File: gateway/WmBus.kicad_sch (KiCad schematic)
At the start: 9 parts, among them IC1201 MIC5317-3.3xM5

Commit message: Working on version 1.0
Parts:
- added C1203, C1204: 100n, Capacitor_SMD:C_0805_2012Metric, symbol Device:C
- added IC1202: TXU0102, Package_SO:VSSOP-8_2.3x2mm_P0.5mm, symbol Texas Instruments:TXU0102
- added M1201: iM891A-XL, IMST:iM891A-XL, symbol IMST:iM891A-XL
- added Q1201: BSS123, Package_TO_SOT_SMD:SOT-23, symbol Transistor_FET:BSS123
- added R1203, R1204, R1206, R1207: 0R, Resistor_SMD:R_0805_2012Metric, symbol Device:R
- added R1205, R1208: 10k, Resistor_SMD:R_0805_2012Metric, symbol Device:R
- added TP1203, TP1204, TP1205, TP1206: ~, Testpoints_Kampi:TestPoint_Pad_1.0x1.0mm, symbol Connector:TestPoint
- C1201, C1202: footprint (none) -> Capacitor_SMD:C_0805_2012Metric; manf (none) -> KYOCERA AVX; manf# (none) -> 08056C105MAT2A; mouser# (none) -> 581-08056C105MAT2A
- IC1201: manf (none) -> Microchip Technology; manf# (none) -> MIC5317-3.3YM5-TR; mouser# (none) -> 998-MIC5317-3.3YM5-TR
- R1201: footprint (none) -> Resistor_SMD:R_0805_2012Metric; manf (none) -> Bourns; manf# (none) -> CR0805-FX-1002GLF; mouser# (none) -> 652-CR0805-FX-1002GLF
- R1202: manf# CR0402-JW-680GLF -> CR0805-JW-680GLF; mouser# 652-CR0402-JW-680GLF -> 652-CR0805-JW-680GLF
- TP1201, TP1202: footprint (none) -> Testpoints_Kampi:TestPoint_Pad_1.0x1.0mm
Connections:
- net +3V3: now also C1204.1, IC1202.7 (VCCB), M1201.29 (VDD), R1208.1
- net GND: now also C1203.2, C1204.2, IC1202.2 (GND), M1201.15 (GND), M1201.17 (GND), M1201.24 (GND), M1201.28 (GND), M1201.30 (GND), M1201.31 (GND), M1201.32 (GND), M1201.33 (GND), M1201.34 (GND), M1201.35 (GND), M1201.5 (GND), Q1201.2 (S), R1205.2
- net wm-Bus-Power-Enable renamed wM-Bus-Power-Enable
- new net: M1201.25 (~{RESET}), Q1201.3 (D), R1208.2, TP1204.1
- new net: M1201.18 (RxD), R1207.2, TP1206.1
- new net: IC1202.8 (B1), R1206.1
- new net: M1201.19 (TxD), R1206.2, TP1205.1
- new net: IC1202.1 (B2), R1207.1
- new net: IC1202.4 (A2), R1204.2
- new net: IC1202.5 (A1), R1203.2
- new net +1V8: C1203.1, IC1202.3 (VCCA), IC1202.6 (OE)
- new net wM-Bus.Reset: Q1201.1 (G), R1205.1, TP1203.1
- new net wM-Bus.RxD: R1204.1
- new net wM-Bus.TxD: R1203.1
- no-connect marks 1 -> 5
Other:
- moved on the sheet: LED1201, R1202

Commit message: Working on PCB
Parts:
- added MP1201: (no value), Bivar:SLP3-300-100-F, symbol Mechanical_Kampi:Light_Pipe

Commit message: Working on version 1.0.0
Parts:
- removed IC1202: TXU0102, Package_SO:VSSOP-8_2.3x2mm_P0.5mm, symbol Texas Instruments:TXU0102
- added IC1202: TXB0104RUT, Package_DFN_QFN:Texas_R-PUQFN-N12, symbol Logic_LevelTranslator:TXB0104RUT
- R1203, R1204: now not fitted; now left out of the parts list
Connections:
- net +1V8: now also C1204.1, IC1202.1 (VCCA), IC1202.12 (OE); no longer C1203.1
- net +3V3: now also C1203.1, IC1202.11 (VCCB); no longer C1204.1
- net GND: now also IC1202.6 (GND)
- net wM-Bus.RxD: now also R1207.1; no longer R1204.1
- net wM-Bus.TxD: now also R1206.1; no longer R1203.1
- net at M1201.18 (RxD), TP1206.1: now also IC1202.9 (B2); no longer R1207.2
- net at M1201.19 (TxD), TP1205.1: now also IC1202.10 (B1); no longer R1206.2
- net at R1204.2: now also IC1202.5 (A4)
- net at R1203.2: now also IC1202.4 (A3)
- new net: IC1202.3 (A2), R1207.2
- new net: IC1202.2 (A1), R1206.2
- new net wM-Bus.CTS: R1204.1
- new net wM-Bus.RTS: R1203.1
- no-connect marks 5 -> 7

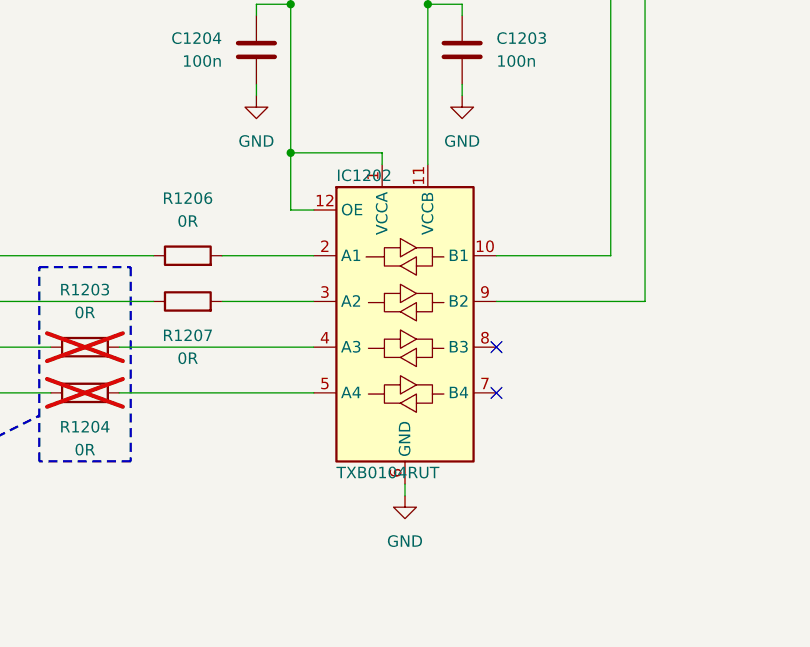
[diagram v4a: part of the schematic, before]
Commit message: Adding level shifter, update documentation
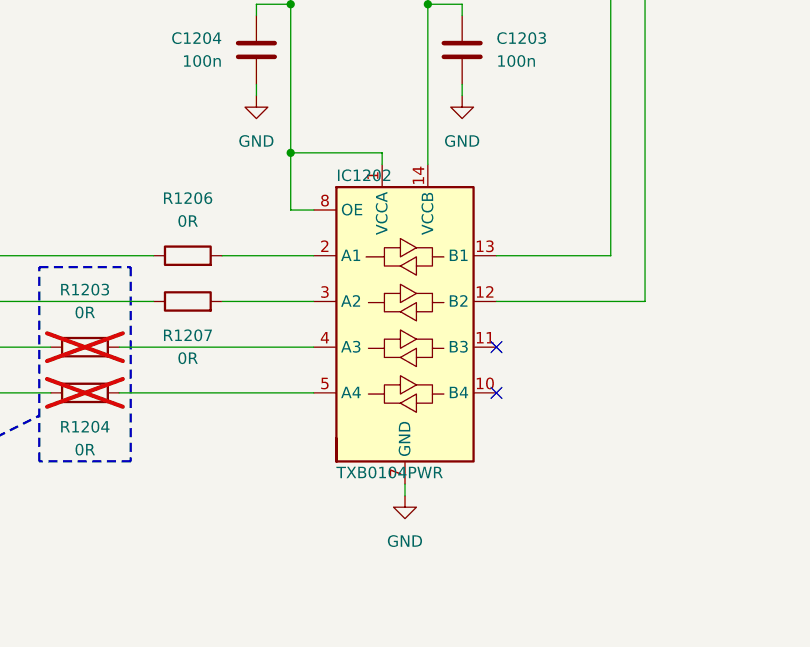
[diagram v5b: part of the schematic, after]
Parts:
- IC1202: value TXB0104RUT -> TXB0104PWR; footprint Package_DFN_QFN:Texas_R-PUQFN-N12 -> Package_SO:TSSOP-14_4.4x5mm_P0.65mm; symbol Logic_LevelTranslator:TXB0104RUT -> Logic_LevelTranslator:TXB0104PW; manf# TXB0104RUTR -> TXB0104PWR; mouser# 595-TXB0104RUTR -> 595-TXB0104PWR
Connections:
- net +1V8: now also IC1202.8 (OE); no longer IC1202.12 (OE)
- net +3V3: now also IC1202.14 (VCCB); no longer IC1202.11 (VCCB)
- net GND: now also IC1202.7 (GND); no longer IC1202.6 (GND)
- net at M1201.18 (RxD), TP1206.1: now also IC1202.12 (B2); no longer IC1202.9 (B2)
- net at M1201.19 (TxD), TP1205.1: now also IC1202.13 (B1); no longer IC1202.10 (B1)
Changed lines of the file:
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@@
 	)
 	(symbol
-		(lib_id "Logic_LevelTranslator:TXB0104RUT")
+		(lib_id "Logic_LevelTranslator:TXB0104PW")
 		(at 185.42 176.53 0)
 		(unit 1)
@@
 			)
 		)
-		(property "Value" "TXB0104RUT"
+		(property "Value" "TXB0104PWR"
 			(at 177.8 193.04 0)
 			(show_name no)
@@
 			)
 		)
-		(property "Footprint" "Package_DFN_QFN:Texas_R-PUQFN-N12"
+		(property "Footprint" "Package_SO:TSSOP-14_4.4x5mm_P0.65mm"
 			(at 185.42 195.58 0)
 			(hide yes)
@@
 			)
 		)
-		(property "Description" "4-Bit Bidirectional Voltage-Level Translator, Auto Direction Sensing and ±15-kV ESD Protection, 1.2 - 3.6V APort, 1.65 - 5.5V BPort, Texas_PUQFN-12"
+		(property "Description" "4-Bit Bidirectional Voltage-Level Translator, Auto Direction Sensing and ±15-kV ESD Protection, 1.2 - 3.6V APort, 1.65 - 5.5V BPort, TSSOP-14"
 			(at 185.42 176.53 0)
 			(hide yes)
@@
 			)
 		)
-		(property "manf#" "TXB0104RUTR"
+		(property "manf#" "TXB0104PWR"
 			(at 185.42 176.53 0)
 			(hide yes)
@@
 			)
 		)
-		(property "mouser#" "595-TXB0104RUTR"
+		(property "mouser#" "595-TXB0104PWR"
 			(at 185.42 176.53 0)
 			(hide yes)
@@
 		(pin "8"
 		)
+		(pin "13"
+		)
+		(pin "14"
+		)
 		(instances

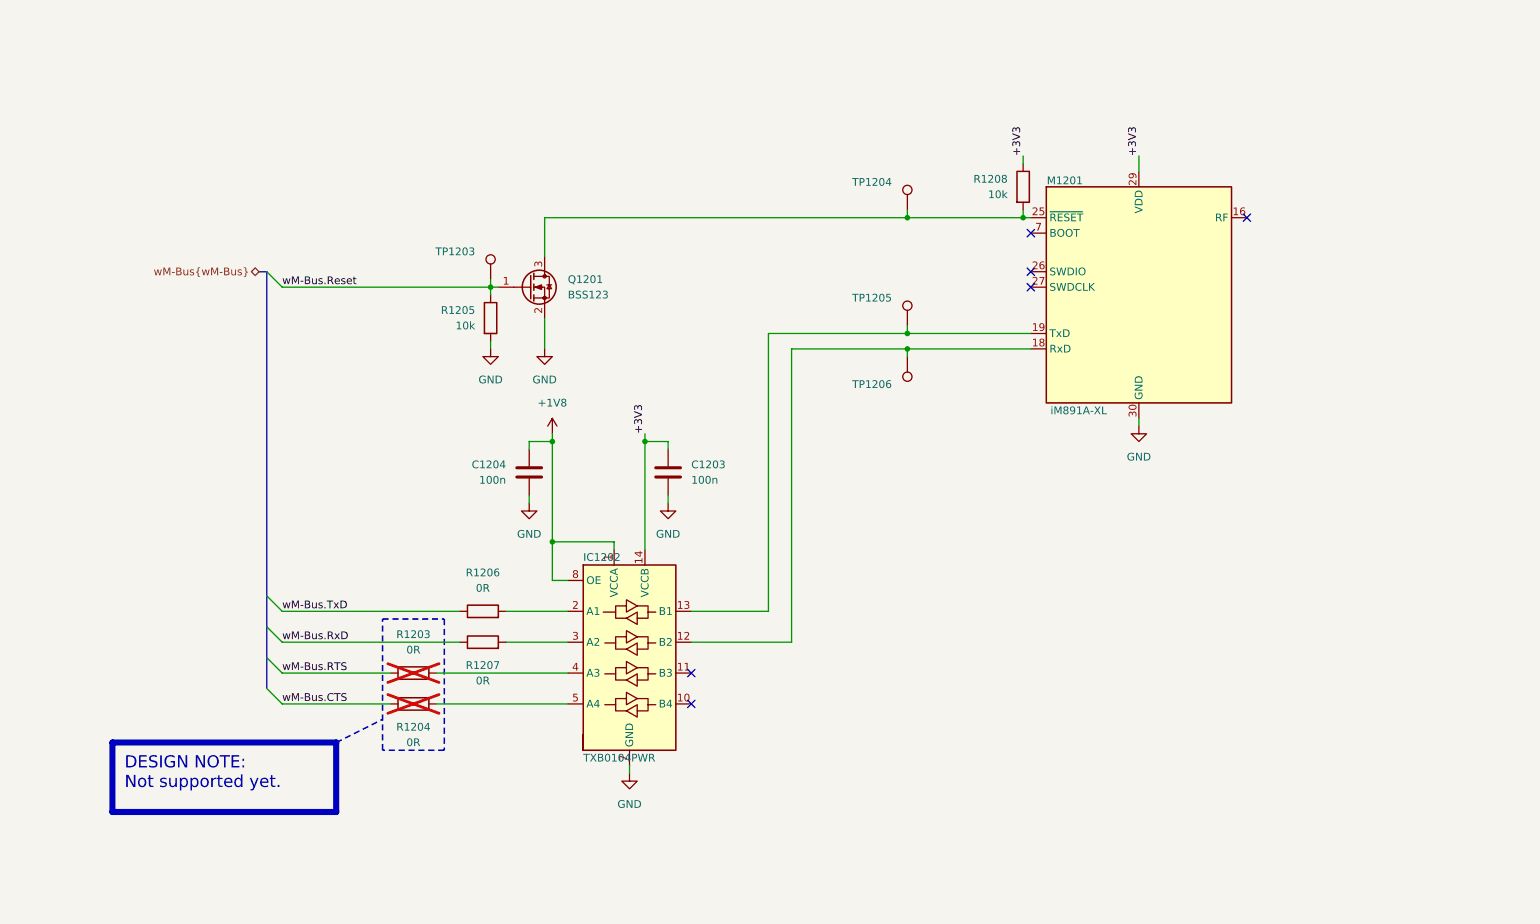
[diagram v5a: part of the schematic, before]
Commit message: Replace level shifter, replace CC2530 with CC2652, fix wrong part numbers
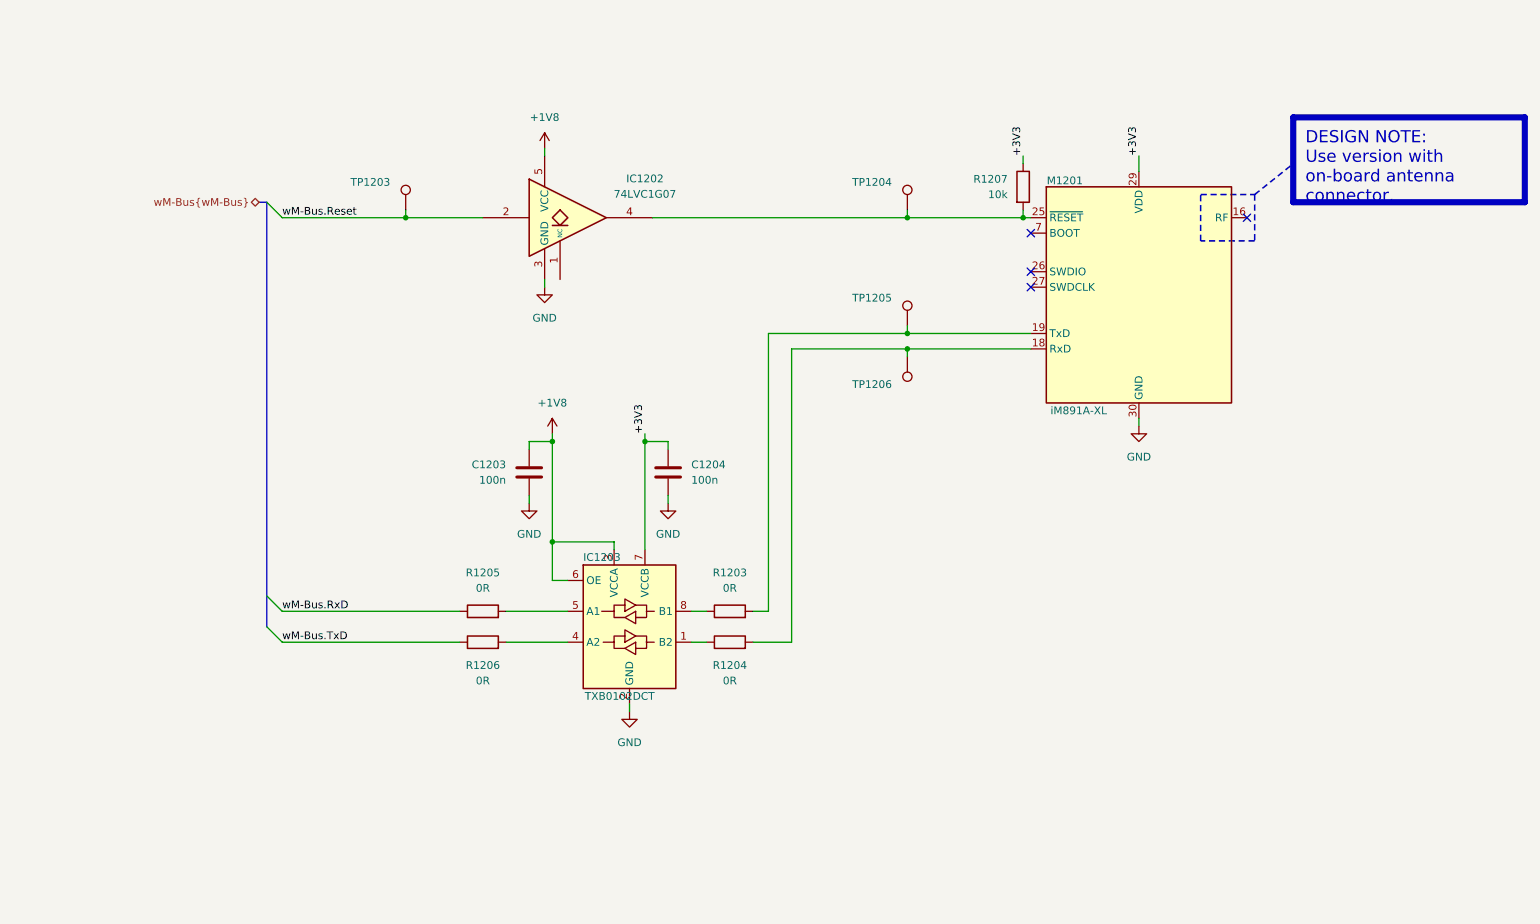
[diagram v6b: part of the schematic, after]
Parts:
- removed IC1202: TXB0104PWR, Package_SO:TSSOP-14_4.4x5mm_P0.65mm, symbol Logic_LevelTranslator:TXB0104PW
- removed Q1201: BSS123, Package_TO_SOT_SMD:SOT-23, symbol Transistor_FET:BSS123
- removed R1205: 10k, Resistor_SMD:R_0805_2012Metric, symbol Device:R
- added IC1202: 74LVC1G07, Package_TO_SOT_SMD:SOT-353_SC-70-5, symbol 74xGxx:74LVC1G07
- added IC1203: TXB0102DCT, Package_SO:VSSOP-8_2.3x2mm_P0.5mm, symbol Logic_LevelTranslator:TXB0102DCT
- R1202: footprint Resistor_SMD:R_0402_1005Metric -> Resistor_SMD:R_0805_2012Metric
- R1203, R1204: now fitted; now in the parts list
- renumbered C1204 to C1203, C1203 to C1204, R1206 to R1205, R1207 to R1206, R1208 to R1207
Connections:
- net +1V8: now also IC1202.5 (VCC), IC1203.3 (VCCA), IC1203.6 (OE)
- net +3V3: now also IC1203.7 (VCCB)
- net GND: now also IC1202.3 (GND), IC1203.2 (GND)
- net wM-Bus.Reset: now also IC1202.2
- net wM-Bus.RxD: now also R1205.1; no longer R1206.1
- net wM-Bus.TxD: now also R1206.1; no longer R1205.1
- net at M1201.25 (~{RESET}), R1207.2, TP1204.1: now also IC1202.4
- net at M1201.18 (RxD), TP1206.1: now also R1204.2
- net at M1201.19 (TxD), TP1205.1: now also R1203.2
- net at R1206.2: now also IC1203.4 (A2)
- net at R1205.2: now also IC1203.5 (A1)
- net wM-Bus.CTS: no longer names the net of R1204.1
- net wM-Bus.CTS: now also IC1203.1 (B2)
- net wM-Bus.RTS: no longer names the net of R1203.1
- net wM-Bus.RTS: now also IC1203.8 (B1)
- no-connect marks 7 -> 5
